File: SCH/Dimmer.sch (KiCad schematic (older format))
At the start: 49 parts, among them J2 Conn_01x03, J3 Load (motor), Q1 BT137S, U1 MOC3023M, U2 LNK3206D

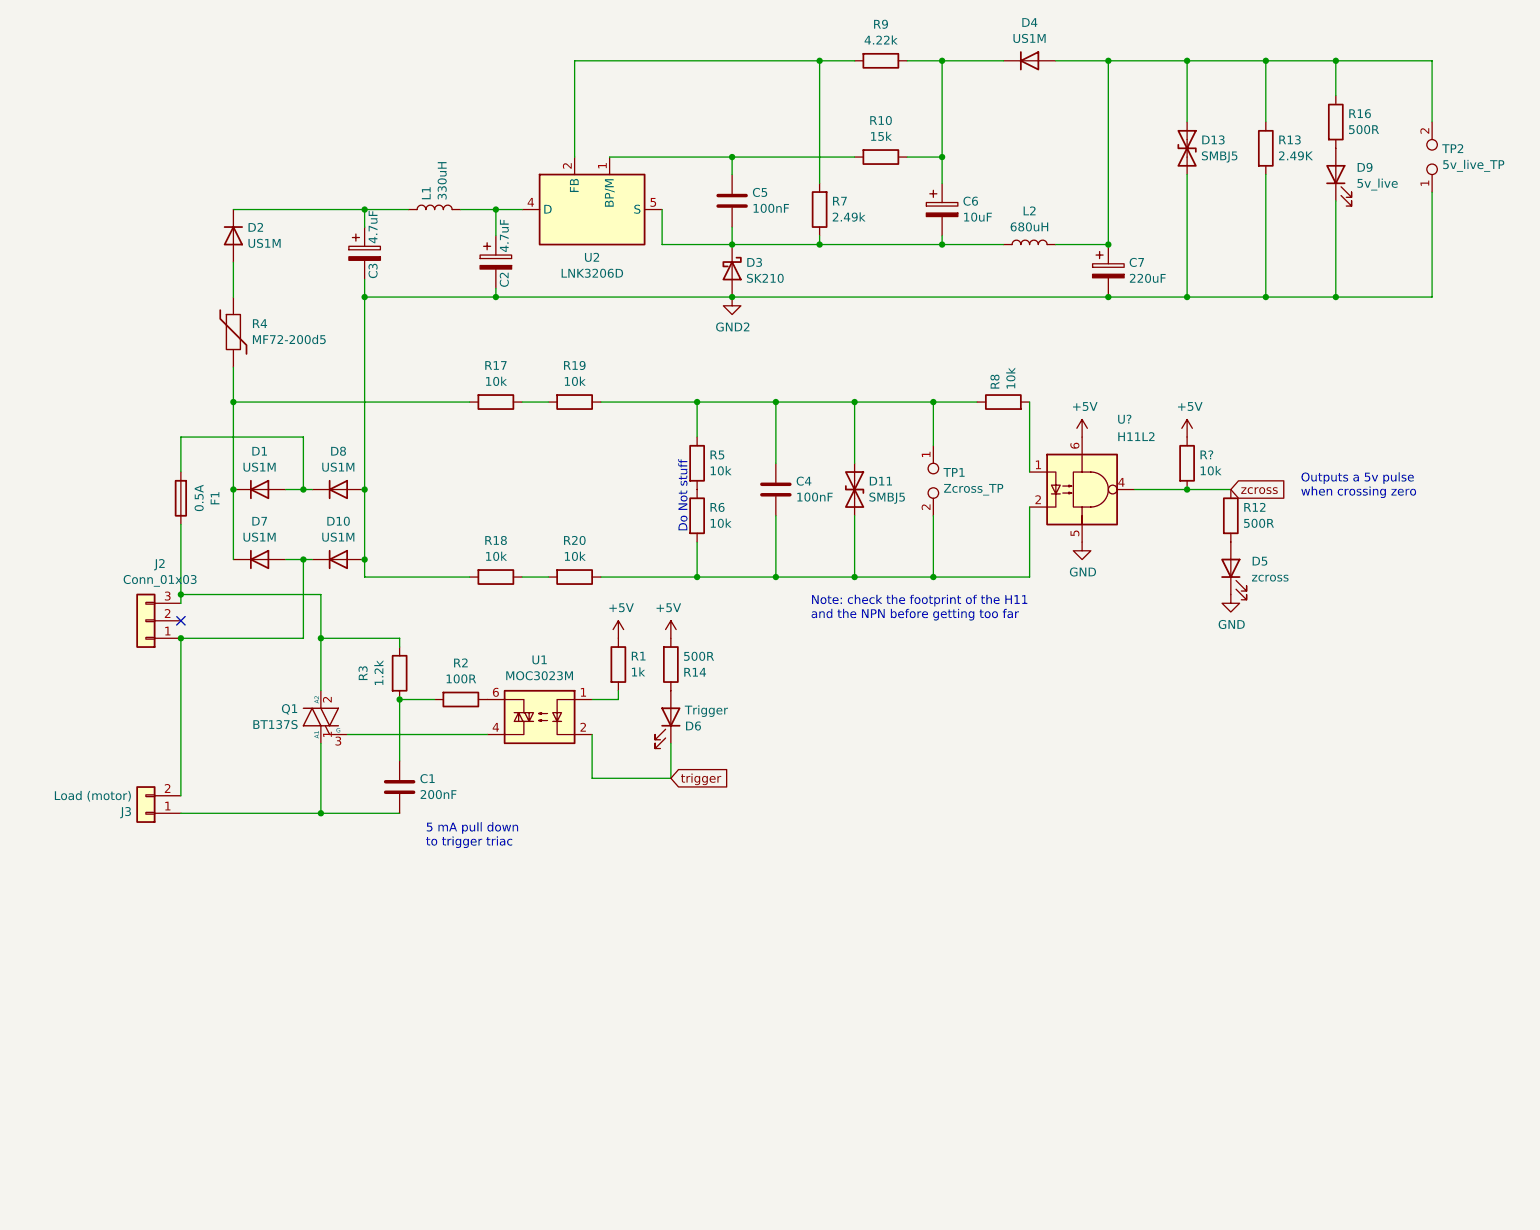
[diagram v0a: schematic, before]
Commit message: Removed backup software, changed schematic to improve circuit. No change on PCB.
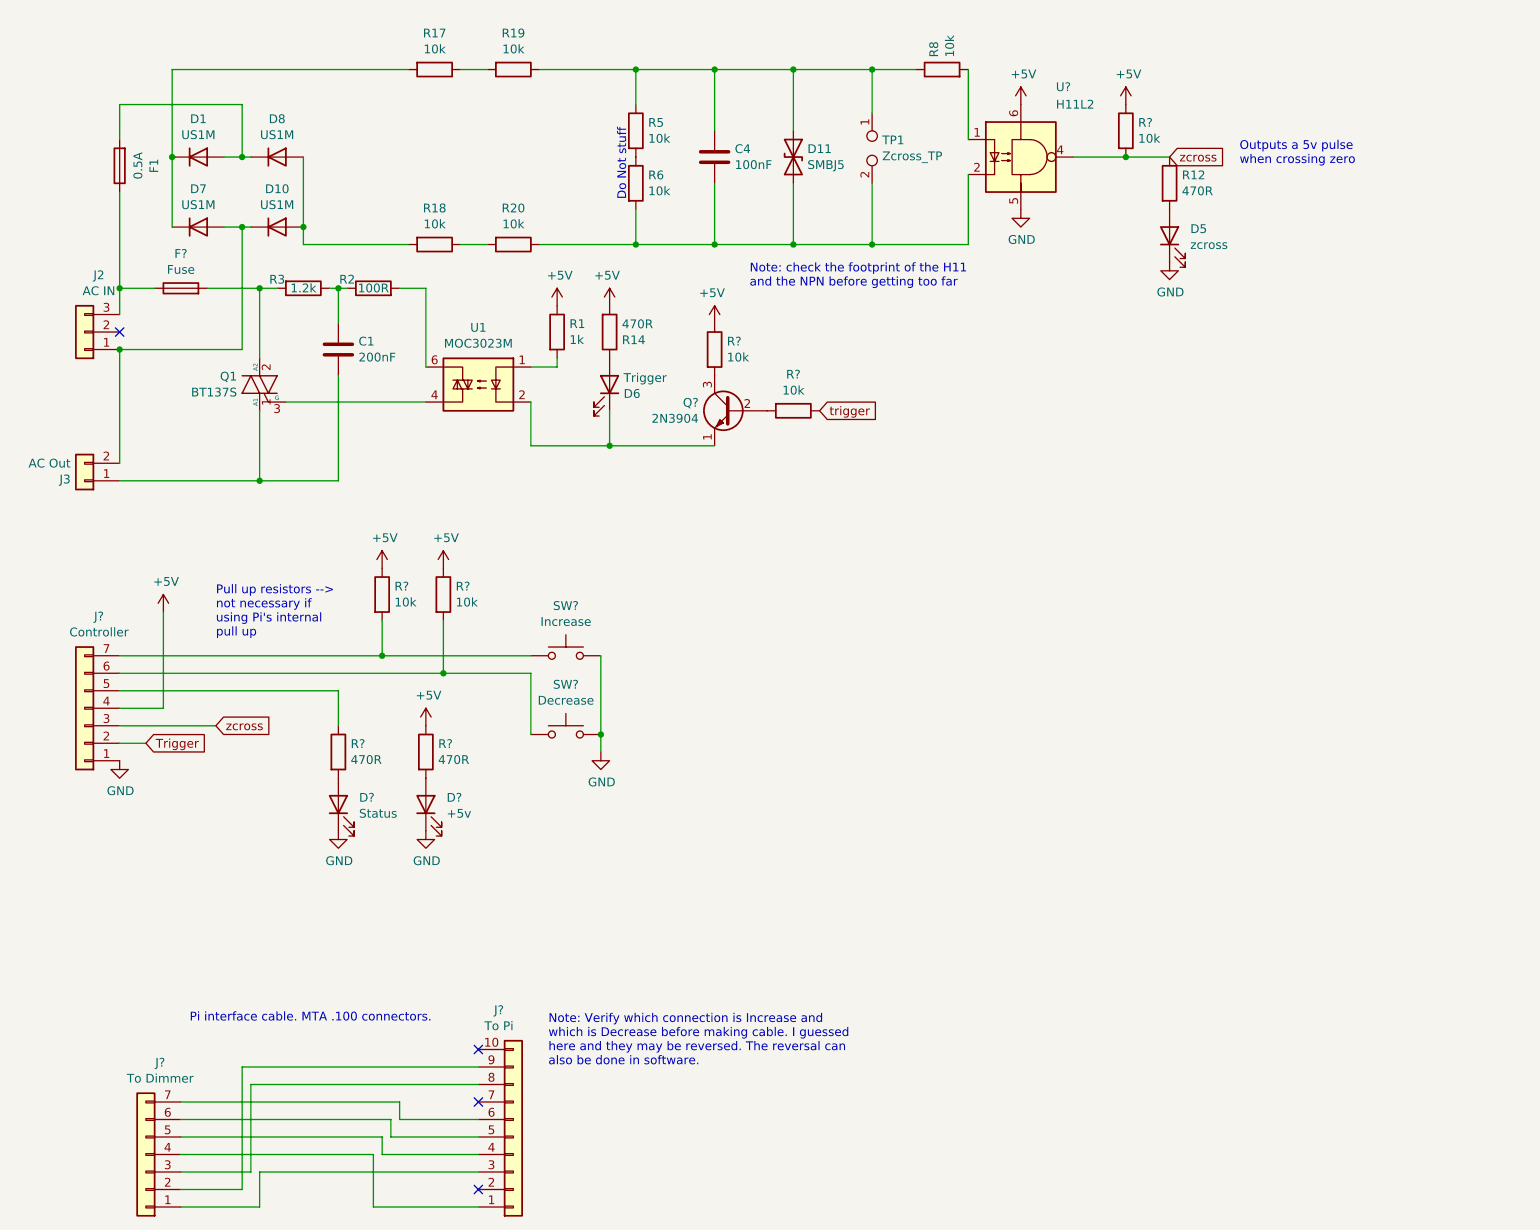
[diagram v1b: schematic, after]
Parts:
- removed C2, C3: 4.7uF, Capacitor_SMD:CP_Elec_8x10, symbol Device:CP
- removed C5: 100nF, Capacitor_SMD:C_1206_3216Metric, symbol Device:C
- removed C6: 10uF, Capacitor_THT:CP_Radial_D4.0mm_P2.00mm, symbol Device:CP
- removed C7: 220uF, Capacitor_THT:CP_Radial_D5.0mm_P2.50mm, symbol Device:CP
- removed D13: SMBJ5, Diode_SMD:D_SMB, symbol Device:D_TVS
- removed D2, D4: US1M, Diode_SMD:D_SMA, symbol Diode:US1M
- removed D3: SK210, Diode_SMD:D_SMA-SMB_Universal_Handsoldering, symbol Device:D_Schottky
- removed D9: 5v_live, LED_THT:LED_D5.0mm, symbol Device:LED
- removed L1: 330uH, Inductor_SMD:L_Wuerth_HCI-1030, symbol Device:L
- removed L2: 680uH, Inductor_SMD:L_Wuerth_HCI-1030, symbol Device:L
- removed R10: 15k, Resistor_SMD:R_1206_3216Metric, symbol Device:R
- removed R13: 2.49K, Resistor_SMD:R_1206_3216Metric, symbol Device:R
- removed R16: 500R, Resistor_SMD:R_1206_3216Metric, symbol Device:R
- removed R4: MF72-200d5, Capacitor_THT:C_Disc_D5.0mm_W2.5mm_P2.50mm, symbol Device:Thermistor
- removed R7: 2.49k, Resistor_SMD:R_1206_3216Metric, symbol Device:R
- removed R9: 4.22k, Resistor_SMD:R_1206_3216Metric, symbol Device:R
- removed TP2: 5v_live_TP, Connector_PinHeader_2.54mm:PinHeader_1x02_P2.54mm_Vertical, symbol Connector:TestPoint_2Pole
- removed U2: LNK3206D, Package_SO:PowerIntegrations_SO-8C, symbol Regulator_Switching:LNK3206D
- added D?: Status, symbol Device:LED
- added D?: +5v, symbol Device:LED
- added F?: Fuse, symbol Device:Fuse
- added J?: Controller, symbol Connector_Generic:Conn_01x07
- added J?: To Dimmer, symbol Connector_Generic:Conn_01x07
- added J?: To Pi, symbol Connector_Generic:Conn_01x10
- added Q?: 2N3904, Package_TO_SOT_THT:TO-92_Inline, symbol Transistor_BJT:2N3904
- added R? (x2): 470R, symbol Device:R
- added R? (x4): 10k, symbol Device:R
- added SW?: Increase, symbol Switch:SW_Push
- added SW?: Decrease, symbol Switch:SW_Push
- J2: value Conn_01x03 -> AC IN
- J3: value Load (motor) -> AC Out
- R12, R14: value 500R -> 470R
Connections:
- net +5V: now also J?.4 (Pin_4), R?.1, R?.1, R?.1, R?.1
- net GND: now also D?.1 (K), D?.1 (K), J?.1 (Pin_1), SW?.2, SW?.2
- net trigger: now also R?.1; no longer D6.1 (K), U1.2
- net zcross: now also J?.3 (Pin_3)
- net at U1.6: now also R2.2; no longer R2.1
- net at F1.1, J2.3 (Pin_3): now also F?.1; no longer Q1.2 (A2), R3.1
- net GND2: no longer names the net of D10.2 (A), D8.2 (A), R18.2
- new net: D6.1 (K), Q?.1 (E), U1.2
- new net: C1.1, R2.1, R3.1
- new net: F?.2, Q1.2 (A2), R3.2
- new net: J?.5 (Pin_5), R?.1
- new net: D?.2 (A), R?.2 (x2)
- new net: J?.6 (Pin_6), R?.2, SW?.1
- new net: J?.7 (Pin_7), R?.2, SW?.1
- new net: Q?.2 (B), R?.2
- new net: Q?.3 (C), R?.2
- new net: J?.1 (Pin_1), J?.3 (Pin_3)
- new net: J?.2 (Pin_2), J?.9 (Pin_9)
- new net: J?.3 (Pin_3), J?.8 (Pin_8)
- new net: J?.1 (Pin_1), J?.4 (Pin_4)
- new net: J?.4 (Pin_4), J?.5 (Pin_5)
- new net: J?.5 (Pin_5), J?.6 (Pin_6)
- new net: J?.6 (Pin_6), J?.7 (Pin_7)
- new net Trigger: J?.2 (Pin_2)
- no-connect marks 1 -> 4
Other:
- note added: "Note: Verify which connection is Increase and \nwhich is Decrease before making cable. I guessed\nhere and they may be reversed. The reversal can\nalso be done in software."
- note added: "Pi interface cable. MTA .100 connectors."
- note added: "Pull up resistors -->\nnot necessary if\nusing Pi's internal \npull up"
- note removed: "5 mA pull down \nto trigger triac"
- moved on the sheet: C1, C4, D1, D10, D11, D5, D6, D7, D8, F1, J2, J3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

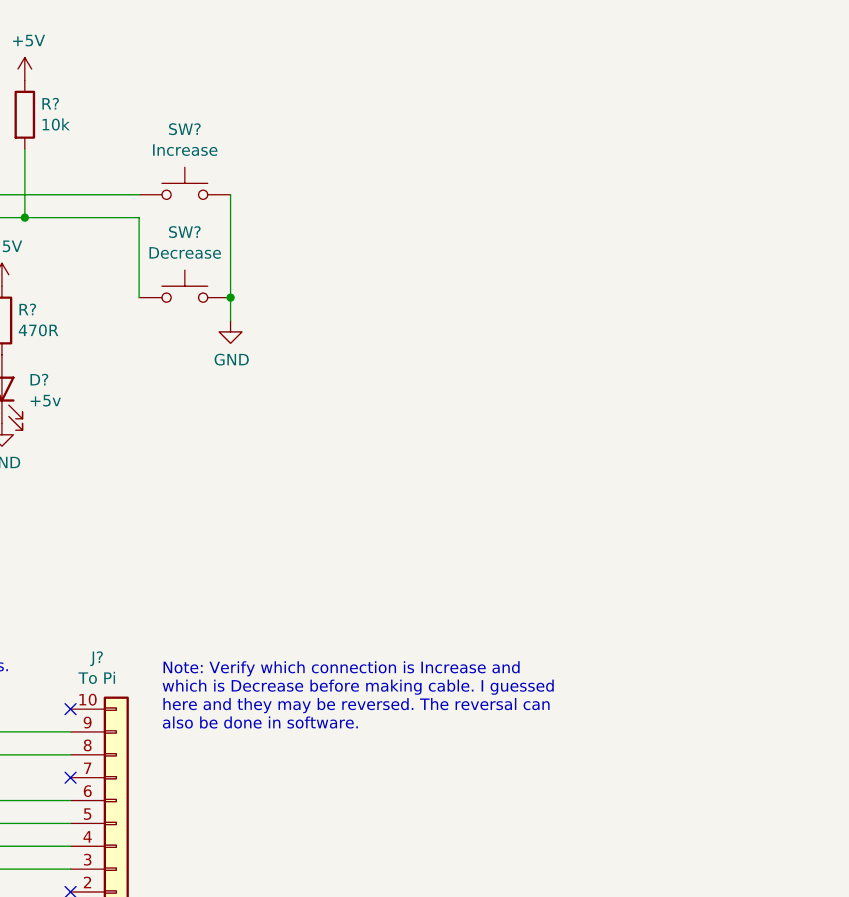
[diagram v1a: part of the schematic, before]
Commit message: Updated schematic, software to clarify speed buttons
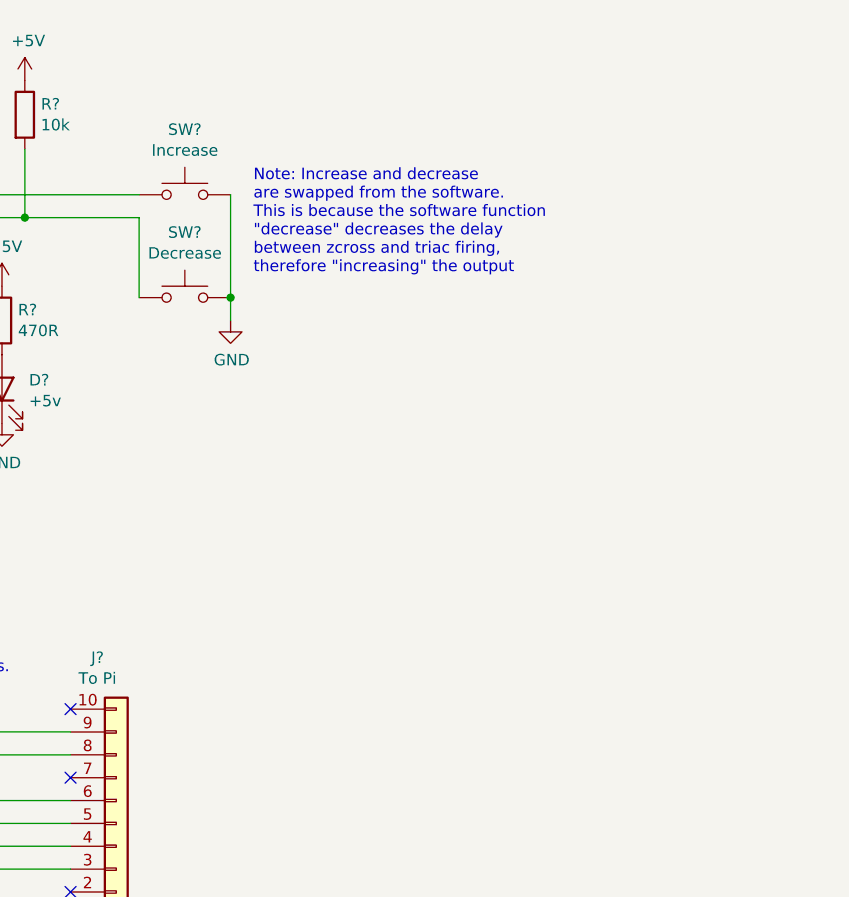
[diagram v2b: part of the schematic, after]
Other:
- note added: "Note: Increase and decrease\nare swapped from the software.\nThis is because the software function\n"decrease" decreases the delay \nbetween zcross and triac firing,\ntherefore "increasing" the output"
- note removed: "Note: Verify which connection is Increase and \nwhich is Decrease before making cable. I guessed\nhere and they may be reversed. The reversal can\nalso be done in software."
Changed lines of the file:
@@
 Wire Wire Line
 	2800 6850 1550 6850
-Text Notes 3650 6650 0    50   ~ 0
-Note: Verify which connection is Increase and \nwhich is Decrease before making cable. I guessed\nhere and they may be reversed. The reversal can\nalso be done in software.
 Wire Wire Line
 	1550 7250 1950 7250
@@
 Text Notes 1600 6400 0    50   ~ 0
 Pi interface cable. MTA .100 connectors.
+Text Notes 4050 4650 0    50   ~ 0
+Note: Increase and decrease\nare swapped from the software.\nThis is because the software function\n"decrease" decreases the delay \nbetween zcross and triac firing,\ntherefore "increasing" the output
 $EndSCHEMATC

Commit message: Latest version before switching PCs
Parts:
- removed Q?: 2N3904, Package_TO_SOT_THT:TO-92_Inline, symbol Transistor_BJT:2N3904
- added Q?: 2n3702, symbol Device:Q_PNP_BCE
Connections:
- net GND: now also Q?.2 (C)
- net at D6.1 (K), U1.2: now also Q?.3 (E)
- net at R?.2: now also R?.2, Q?.1 (B)
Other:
- moved on the sheet: R?
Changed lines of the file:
@@
 Text GLabel 7200 1450 2    50   Input ~ 0
 zcross
-Text GLabel 5200 2900 2    50   Input ~ 0
-trigger
 $Comp
 L Connector:TestPoint_2Pole TP1
@@
 	2250 1950 2850 1950
 Connection ~ 2250 1850
-Text Notes 4800 2200 0    50   ~ 0
+Text Notes 4700 2600 0    50   ~ 0
 Note: check the footprint of the H11\nand the NPN before getting too far
 $Comp
@@
 	2450 4700 2450 4500
 $Comp
-L Device:R R?
-U 1 1 5F49F503
-P 5050 2900
-F 0 "R?" V 4843 2900 50  0000 C CNN
-F 1 "10k" V 4934 2900 50  0000 C CNN
-F 2 "" V 4980 2900 50  0001 C CNN
-F 3 "~" H 5050 2900 50  0001 C CNN
-	1    5050 2900
-	0    1    1    0
-$EndComp
-$Comp
-L Transistor_BJT:2N3904 Q?
-U 1 1 5F4A0172
-P 4700 2900
-F 0 "Q?" H 4891 2946 50  0000 L CNN
-F 1 "2N3904" H 4891 2855 50  0000 L CNN
-F 2 "Package_TO_SOT_THT:TO-92_Inline" H 4900 2825 50  0001 L CIN
-F 3 "https://www.fairchildsemi.com/datasheets/2N/2N3904.pdf" H 4700 2900 50  0001 L CNN
-	1    4700 2900
-	-1   0    0    -1
-$EndComp
-$Comp
-L Device:R R?
-U 1 1 5F4ACCEA
-P 4600 2550
-F 0 "R?" H 4670 2596 50  0000 L CNN
-F 1 "10k" H 4670 2505 50  0000 L CNN
-F 2 "" V 4530 2550 50  0001 C CNN
-F 3 "~" H 4600 2550 50  0001 C CNN
-	1    4600 2550
-	1    0    0    -1
-$EndComp
-Wire Wire Line
-	4600 3100 4000 3100
-Connection ~ 4000 3100
-$Comp
-L power:+5V #PWR?
-U 1 1 5F4B2C88
-P 4600 2400
-F 0 "#PWR?" H 4600 2250 50  0001 C CNN
-F 1 "+5V" H 4615 2573 50  0000 C CNN
-F 2 "" H 4600 2400 50  0001 C CNN
-F 3 "" H 4600 2400 50  0001 C CNN
-	1    4600 2400
-	-1   0    0    -1
-$EndComp
-$Comp
 L Connector_Generic:Conn_01x07 J?
 U 1 1 5F4B9853
@@
 Text Notes 4050 4650 0    50   ~ 0
 Note: Increase and decrease\nare swapped from the software.\nThis is because the software function\n"decrease" decreases the delay \nbetween zcross and triac firing,\ntherefore "increasing" the output
+$Comp
+L power:+5V #PWR?
+U 1 1 5F4B2C88
+P 4550 2800
+F 0 "#PWR?" H 4550 2650 50  0001 C CNN
+F 1 "+5V" H 4565 2973 50  0000 C CNN
+F 2 "" H 4550 2800 50  0001 C CNN
+F 3 "" H 4550 2800 50  0001 C CNN
+	1    4550 2800
+	-1   0    0    -1
+$EndComp
+$Comp
+L Device:R R?
+U 1 1 5F4ACCEA
+P 4550 2950
+F 0 "R?" H 4620 2996 50  0000 L CNN
+F 1 "10k" H 4620 2905 50  0000 L CNN
+F 2 "" V 4480 2950 50  0001 C CNN
+F 3 "~" H 4550 2950 50  0001 C CNN
+	1    4550 2950
+	1    0    0    -1
+$EndComp
+$Comp
+L Device:R R?
+U 1 1 5F49F503
+P 4900 3300
+F 0 "R?" V 4693 3300 50  0000 C CNN
+F 1 "10k" V 4784 3300 50  0000 C CNN
+F 2 "" V 4830 3300 50  0001 C CNN
+F 3 "~" H 4900 3300 50  0001 C CNN
+	1    4900 3300
+	0    1    1    0
+$EndComp
+Text GLabel 5050 3300 2    50   Input ~ 0
+trigger
+$Comp
+L power:GND #PWR?
+U 1 1 5F4FC040
+P 4000 3500
+F 0 "#PWR?" H 4000 3250 50  0001 C CNN
+F 1 "GND" H 4005 3327 50  0000 C CNN
+F 2 "" H 4000 3500 50  0001 C CNN
+F 3 "" H 4000 3500 50  0001 C CNN
+	1    4000 3500
+	1    0    0    -1
+$EndComp
+Wire Wire Line
+	4550 3100 4550 3300
+Wire Wire Line
+	4550 3300 4750 3300
+Wire Wire Line
+	4300 3300 4550 3300
+Connection ~ 4550 3300
+$Comp
+L Device:Q_PNP_BCE Q?
+U 1 1 5F514AFA
+P 4100 3300
+F 0 "Q?" H 4291 3254 50  0000 L CNN
+F 1 "2n3702" H 4291 3345 50  0000 L CNN
+F 2 "" H 4300 3400 50  0001 C CNN
+F 3 "~" H 4100 3300 50  0001 C CNN
+	1    4100 3300
+	-1   0    0    1
+$EndComp
+Connection ~ 4000 3100
 $EndSCHEMATC
